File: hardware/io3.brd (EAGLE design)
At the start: 98.1 x 60.3 mm, 37 parts, among them IC2 74HC14D, IC3 74HC74D, Q1 BC857BSMD, U1 TXB0108PWR

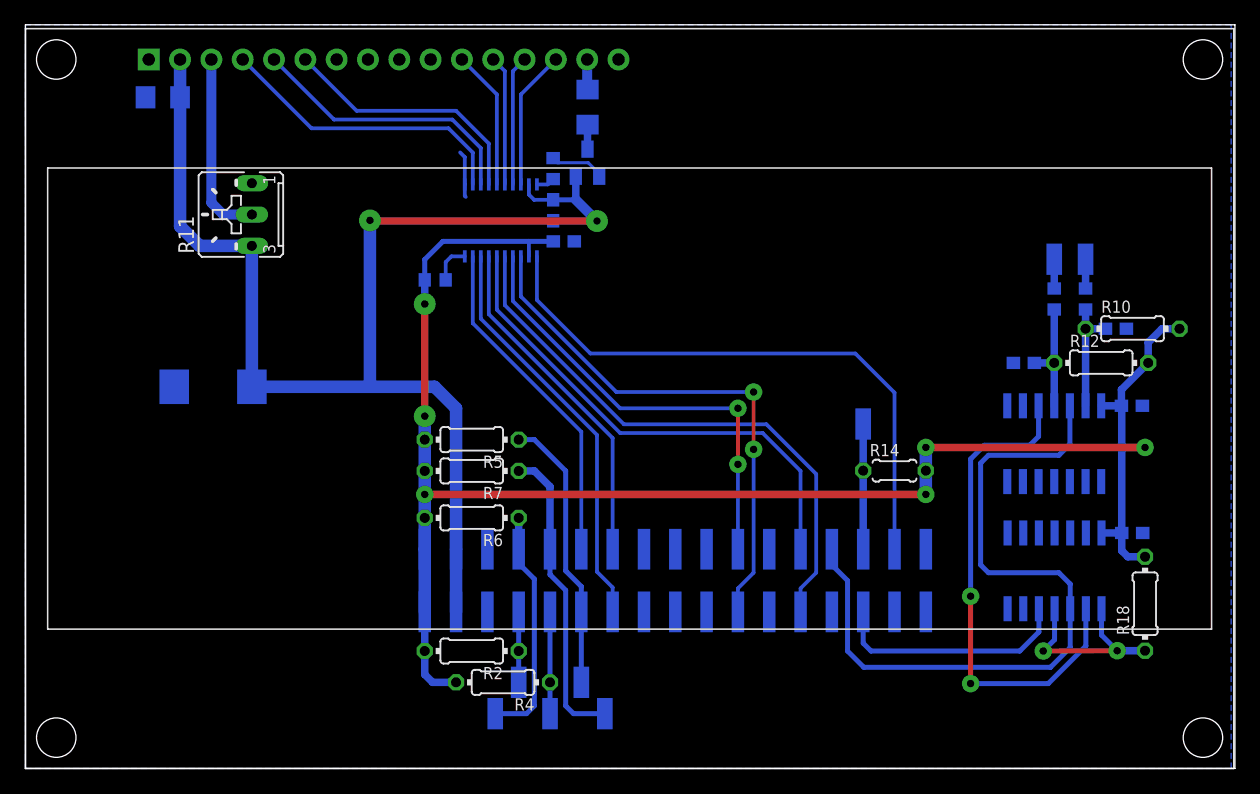
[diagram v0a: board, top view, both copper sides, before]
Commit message: io3 board fix - no need to twist lines in ribbon
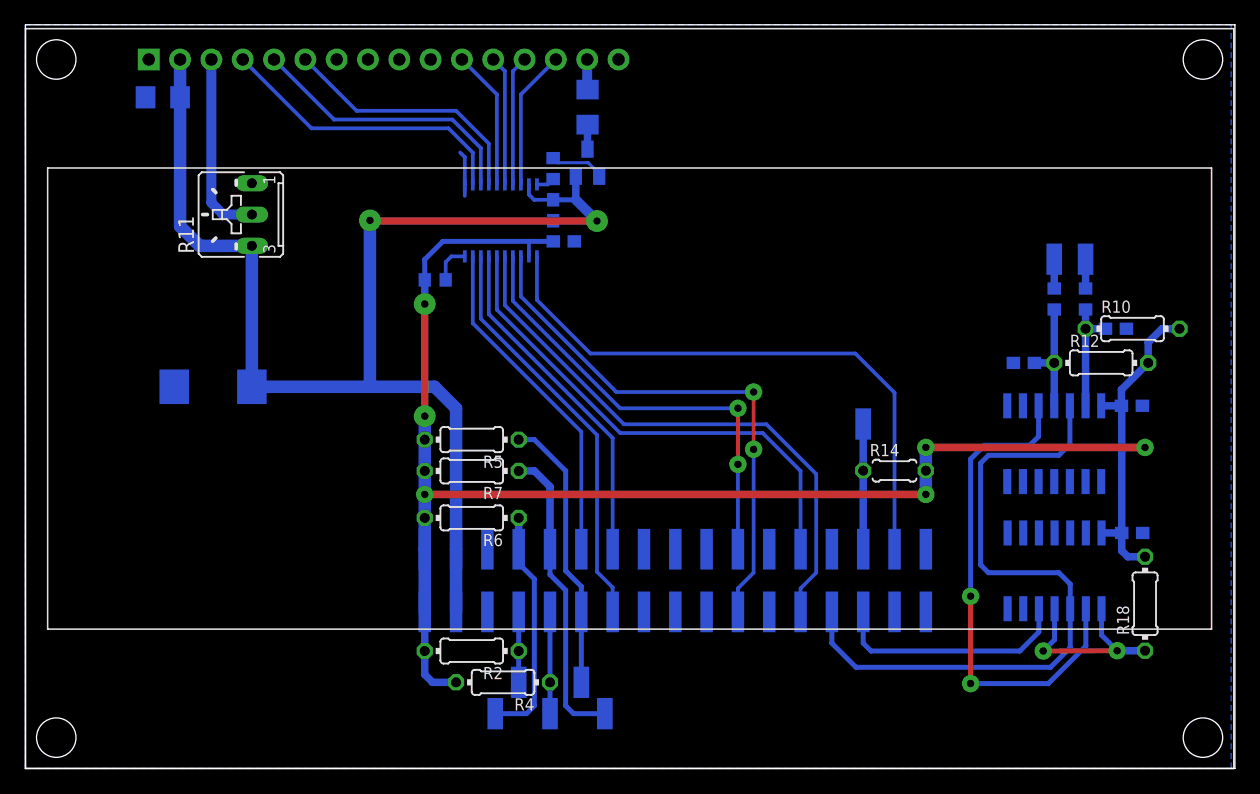
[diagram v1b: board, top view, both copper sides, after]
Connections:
- net ROT_STEP: now also JP1.7; no longer JP1.8
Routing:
- net ROT_STEP: track 60.4 -> 55.7 mm
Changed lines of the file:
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@@
 <wire x1="35.6322" y1="49.5848" x2="35.2552" y2="49.9618" width="0.3048" layer="16"/>
 <wire x1="35.6322" y1="47.3678" x2="35.6322" y2="46.4352" width="0.3048" layer="16"/>
-<wire x1="35.6322" y1="46.4352" x2="35.7124" y2="46.355" width="0.3048" layer="16"/>
 </signal>
 <signal name="D4">
@@
 <contactref element="IC3" pad="3"/>
 <wire x1="84.7344" y1="12.954" x2="84.7344" y2="9.8044" width="0.4064" layer="16"/>
-<contactref element="JP1" pad="8"/>
-<wire x1="65.405" y1="17.78" x2="65.405" y2="16.51" width="0.3048" layer="16"/>
-<wire x1="65.405" y1="16.51" x2="66.675" y2="15.24" width="0.4064" layer="16"/>
-<wire x1="66.675" y1="15.24" x2="66.675" y2="9.525" width="0.4064" layer="16"/>
-<wire x1="66.675" y1="9.525" x2="67.9958" y2="8.2042" width="0.4064" layer="16"/>
+<wire x1="65.405" y1="10.16" x2="67.3608" y2="8.2042" width="0.4064" layer="16"/>
 <wire x1="84.7344" y1="12.954" x2="84.7344" y2="14.9606" width="0.4064" layer="16"/>
 <wire x1="84.7344" y1="14.9606" x2="83.82" y2="15.875" width="0.4064" layer="16"/>
@@
 <wire x1="84.709" y1="29.4132" x2="84.709" y2="26.289" width="0.4064" layer="16"/>
 <wire x1="84.7344" y1="9.8044" x2="83.1342" y2="8.2042" width="0.4064" layer="16"/>
-<wire x1="83.1342" y1="8.2042" x2="67.9958" y2="8.2042" width="0.4064" layer="16"/>
+<wire x1="83.1342" y1="8.2042" x2="67.3608" y2="8.2042" width="0.4064" layer="16"/>
+<contactref element="JP1" pad="7"/>
+<wire x1="65.405" y1="10.16" x2="65.405" y2="12.7" width="0.4064" layer="16"/>
 </signal>
 <signal name="ROT_B_">

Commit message: IO PCB updated - no buffer
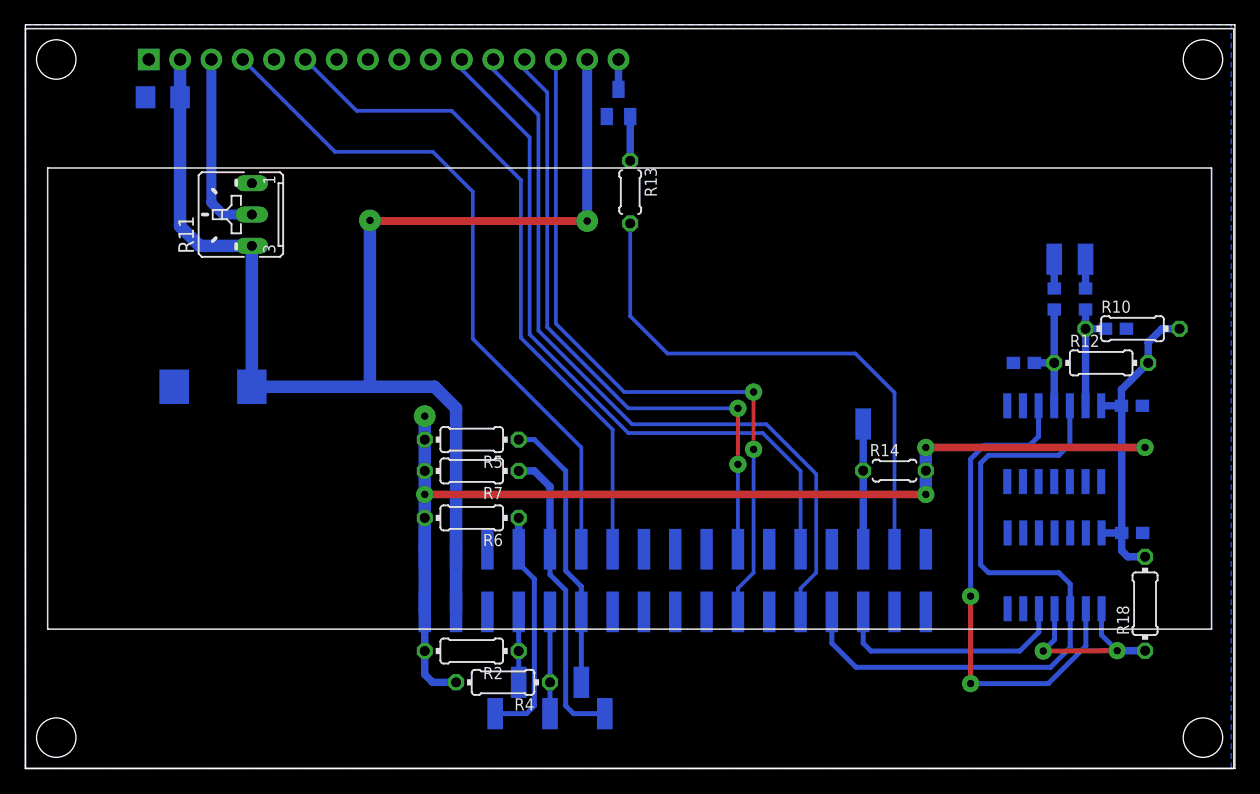
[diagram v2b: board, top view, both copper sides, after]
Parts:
- removed C1, C9: (no value), rcl:C0603
- removed Q1: BC857BSMD, transistor-pnp:SOT23-BEC
- removed R1: (no value), rcl:R0603
- removed R15: (no value), rcl:R1206
- removed U1: TXB0108PWR, microbuilder:TSSOP20
- added T1: BC847, transistor:SOT23
- R13: device rcl:R0603 -> rcl:0204/5
- moved R13 6.53 mm to (49.0, 46.7), flipped to the top
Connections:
- removed net BACKLIGHT: R13.2, U1.20
- removed net D4: U$1.P$11, U1.15
- removed net D5: U$1.P$12, U1.16
- removed net D6: U$1.P$13, U1.17
- removed net D7: U$1.P$14, U1.18
- removed net LCD_EN: U$1.P$6, U1.14
- removed net N$3: R15.2, U$1.P$15
- removed net N$4: R1.1, U1.10
- removed net RS: U$1.P$4, U1.12
- removed net RW: U$1.P$5, U1.13
- net 3V: no longer C9.1, R1.2, U1.2
- net 5V: now also U$1.P$15; no longer C1.1, Q1.E, U1.19
- net BACKLIGHT_RC15: now also R13.2; no longer U1.1
- net D4_RD2: now also U$1.P$11; no longer U1.6
- net D5_RD3: now also U$1.P$12; no longer U1.5
- net D6_RD4: now also U$1.P$13; no longer U1.4
- net D7_RD5: now also U$1.P$14; no longer U1.3
- net GND: now also T1.2, U$1.P$5; no longer C1.2, C9.2, U$1.P$16, U1.11
- net LCD_EN_RE1: now also U$1.P$6; no longer U1.7
- net N$1: now also T1.3, U$1.P$16; no longer Q1.C, R15.1
- net N$6: now also T1.1; no longer Q1.B
- net RS_RG12: now also U$1.P$4; no longer U1.9
- net RW_RG14: no longer U1.8
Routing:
- net RW_RG14: track 33.3 -> 0.00 mm
- net RS_RG12: track 27.4 -> 55.7 mm
- net LCD_EN_RE1: track 27.9 -> 54.6 mm
- net 3V: track 139.0 -> 114.0 mm, vias 6 -> 5
- net RS: track 24.4 -> 0.00 mm
- net RW: track 22.7 -> 0.00 mm
- net LCD_EN: track 21.0 -> 0.00 mm
- net D4_RD2: track 40.7 -> 57.5 mm
- net D5_RD3: track 46.6 -> 62.6 mm
- net D6_RD4: track 36.9 -> 52.1 mm
- net D7_RD5: track 43.7 -> 58.1 mm
- net D7: track 11.3 -> 0.00 mm
- net D4: track 11.3 -> 0.00 mm
- net D6: track 10.5 -> 0.00 mm
- net D5: track 10.5 -> 0.00 mm
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
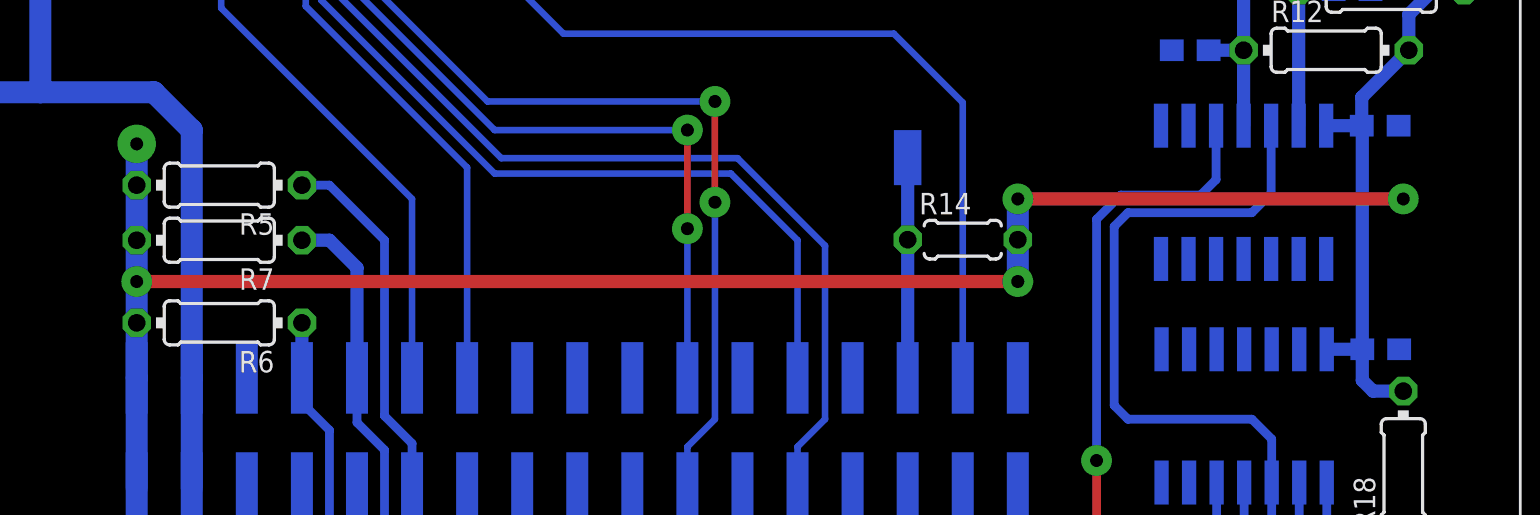
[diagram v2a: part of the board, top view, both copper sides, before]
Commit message: Changes in PCB design allowing us to use bug free I2C1 instead of buggy I2C3
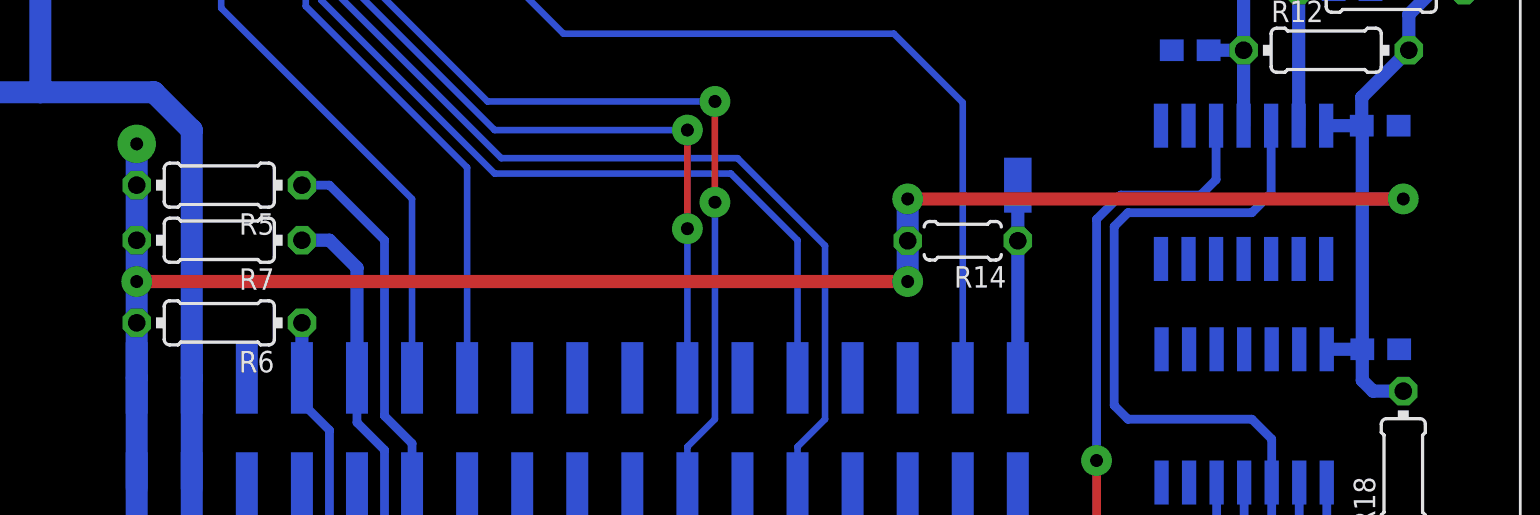
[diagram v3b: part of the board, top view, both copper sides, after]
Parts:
- moved PAD9 5.24 mm to (73.0, 26.7)
- moved R14 0.05 mm to (70.5, 24.1), turned to 180 degrees
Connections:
- net SDA_3V renamed RF8
- removed net SCL_3V: JP1.2
- new net SCL1: JP1.3
- new net SDA1: JP1.6
- net ROT_SW: now also JP1.2; no longer JP1.6
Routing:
- net ROT_SW: track 10.2 -> 8.89 mm
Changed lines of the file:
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@@
 <element name="R10" library="rcl" package="0204/7" value="" x="89.789" y="35.6616"/>
 <element name="R12" library="rcl" package="0204/7" value="" x="87.249" y="32.893"/>
-<element name="R14" library="rcl" package="0204/5" value="" x="70.485" y="24.1554"/>
+<element name="R14" library="rcl" package="0204/5" value="" x="70.485" y="24.1046" rot="R180"/>
 <element name="C2" library="rcl" package="SMC_D" value="" x="15.2146" y="30.955" rot="MR0"/>
 <element name="C4" library="rcl" package="C1206" value="" x="11.14" y="54.4322" rot="MR0"/>
@@
 <element name="PAD2" library="wirepad" package="SMD1,27-2,54" value="" x="38.1" y="4.445" rot="MR0"/>
 <element name="PAD3" library="wirepad" package="SMD1,27-2,54" value="" x="46.99" y="4.445" rot="MR0"/>
-<element name="PAD9" library="wirepad" package="SMD1,27-2,54" value="" x="67.945" y="27.94" rot="MR180"/>
+<element name="PAD9" library="wirepad" package="SMD1,27-2,54" value="" x="73.025" y="26.67" rot="MR180"/>
 <element name="C5" library="rcl" package="C0603" value="" x="88.4428" y="35.6616" rot="MR180"/>
 <element name="C6" library="rcl" package="C0603" value="" x="80.9752" y="32.893" rot="MR0"/>
@@
 <wire x1="49.05" y1="49.284890625" x2="49.05" y2="52.875" width="0.6096" layer="16"/>
 </signal>
-<signal name="SDA_3V">
+<signal name="RF8">
 <contactref element="JP1" pad="1"/>
 <wire x1="73.025" y1="12.7" x2="73.025" y2="13.843" width="0.3048" layer="16"/>
-</signal>
-<signal name="SCL_3V">
-<contactref element="JP1" pad="2"/>
 </signal>
 <signal name="5V">
@@
 <wire x1="32.385" y1="7.62" x2="33.02" y2="6.985" width="0.6096" layer="16"/>
 <wire x1="33.02" y1="6.985" x2="34.925" y2="6.985" width="0.6096" layer="16"/>
-<via x="73.025" y="22.225" extent="1-16" drill="0.6" diameter="1.4224" shape="octagon"/>
-<wire x1="32.385" y1="22.225" x2="73.025" y2="22.225" width="0.6096" layer="1"/>
+<via x="67.945" y="22.225" extent="1-16" drill="0.6" diameter="1.4224" shape="octagon"/>
+<wire x1="32.385" y1="22.225" x2="67.945" y2="22.225" width="0.6096" layer="1"/>
 <contactref element="IC2" pad="14"/>
 <contactref element="C7" pad="1"/>
@@
 <wire x1="90.805" y1="17.1704" x2="89.408" y2="17.1704" width="0.6096" layer="16"/>
 <wire x1="32.385" y1="26.67" x2="32.385" y2="28.5736" width="1.016" layer="16"/>
-<via x="73.025" y="26.035" extent="1-16" drill="0.6" diameter="1.4224" shape="octagon"/>
+<via x="67.945" y="26.035" extent="1-16" drill="0.6" diameter="1.4224" shape="octagon"/>
 <via x="90.805" y="26.035" extent="1-16" drill="0.6" diameter="1.4224" shape="octagon"/>
-<wire x1="73.025" y1="22.225" x2="73.025" y2="24.1554" width="1.016" layer="16"/>
-<wire x1="73.025" y1="24.1554" x2="73.025" y2="26.035" width="1.016" layer="16"/>
+<wire x1="67.945" y1="22.225" x2="67.945" y2="24.1046" width="1.016" layer="16"/>
+<wire x1="67.945" y1="24.1046" x2="67.945" y2="26.035" width="1.016" layer="16"/>
 <wire x1="90.805" y1="26.035" x2="88.9136" y2="26.035" width="0.6096" layer="16"/>
-<wire x1="90.805" y1="26.035" x2="73.025" y2="26.035" width="0.6096" layer="1"/>
+<wire x1="90.805" y1="26.035" x2="67.945" y2="26.035" width="0.6096" layer="1"/>
 <via x="32.385" y="28.5736" extent="1-16" drill="0.6" diameter="1.778" shape="octagon"/>
 <wire x1="32.385" y1="17.78" x2="32.385" y2="20.32" width="1.016" layer="16"/>
@@
 </signal>
 <signal name="ROT_SW">
-<contactref element="JP1" pad="6"/>
 <contactref element="R14" pad="1"/>
 <contactref element="PAD9" pad="1"/>
-<wire x1="67.945" y1="24.1554" x2="67.945" y2="27.94" width="0.6096" layer="16"/>
-<wire x1="67.945" y1="24.1554" x2="67.945" y2="17.78" width="0.6096" layer="16"/>
+<wire x1="73.025" y1="24.1046" x2="73.025" y2="26.67" width="0.6096" layer="16"/>
+<contactref element="JP1" pad="2"/>
+<wire x1="73.025" y1="17.78" x2="73.025" y2="24.1046" width="0.6096" layer="16"/>
 </signal>
 <signal name="ROT_B_CLK">
@@
 <wire x1="48.1" y1="55.075" x2="48.1" y2="57.5" width="0.6096" layer="16"/>
 </signal>
+<signal name="SCL1">
+<contactref element="JP1" pad="3"/>
+</signal>
+<signal name="SDA1">
+<contactref element="JP1" pad="6"/>
+</signal>
 </signals>
